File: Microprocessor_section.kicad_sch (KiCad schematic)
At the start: 13 parts, among them J15 Conn_01x06_Male, SW1 K2-1102SP-C4SC-04, U5 ESP32-WROOM-32D

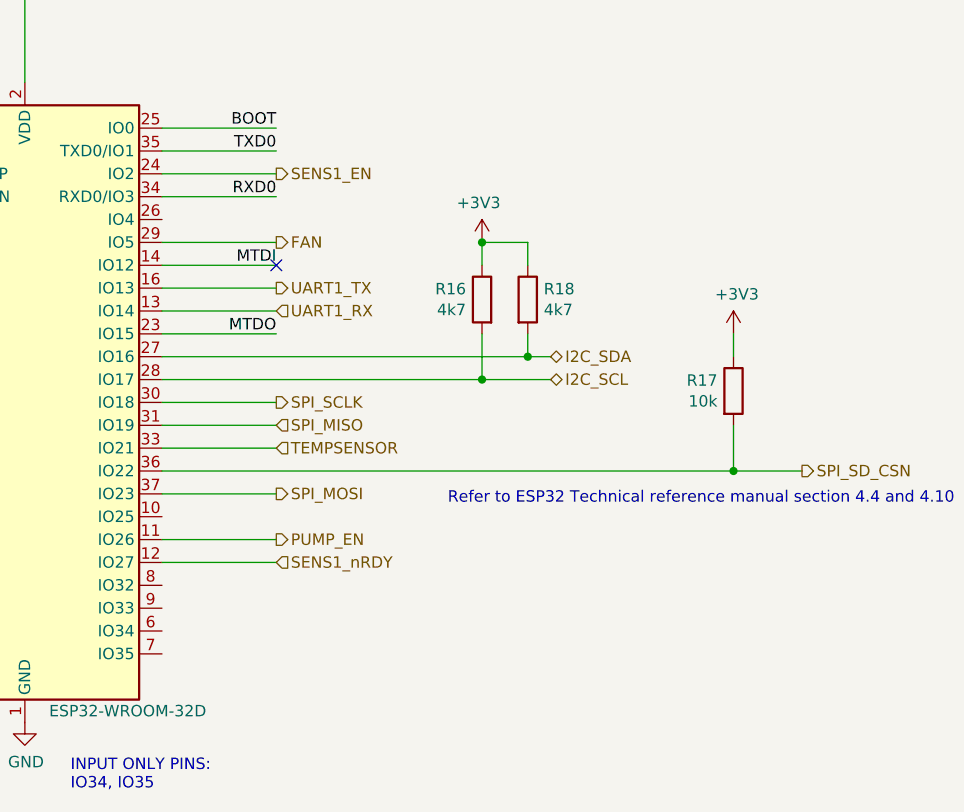
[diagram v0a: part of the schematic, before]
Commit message: Move to KiCad v6, redesign circuit for chamber
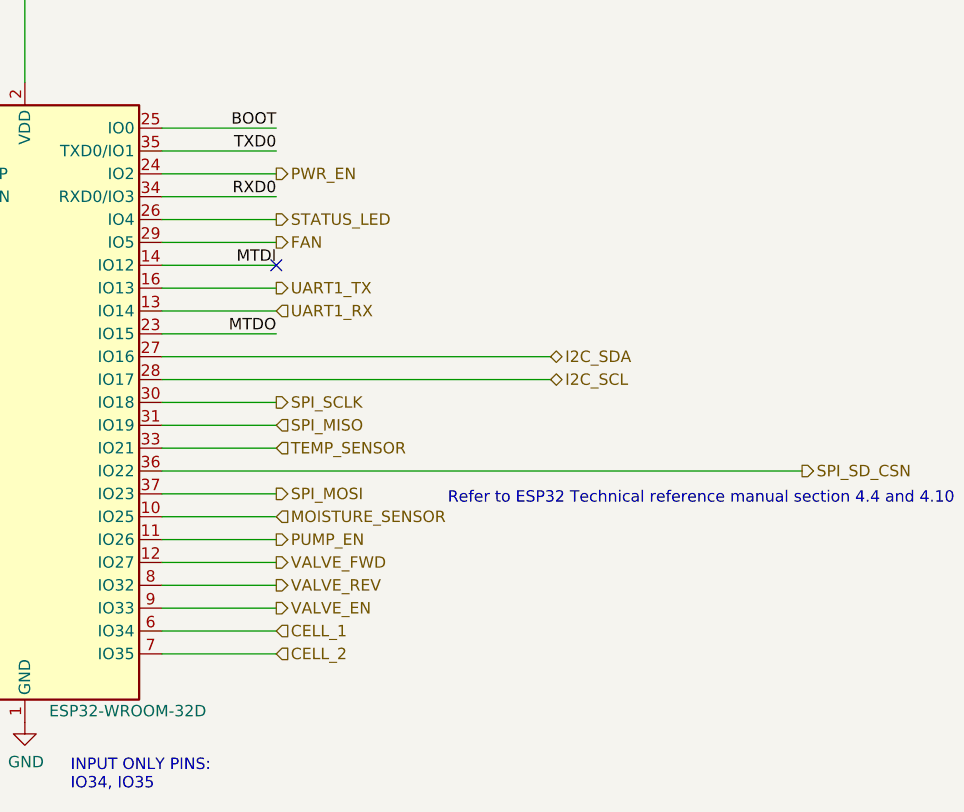
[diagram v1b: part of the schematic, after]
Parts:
- removed R16, R18: 4k7, Resistor_SMD:R_0603_1608Metric, symbol Device:R
- removed R17: 10k, Resistor_SMD:R_0603_1608Metric, symbol Device:R
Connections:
- net MOISTURE_SENSOR: now reaches U5.10 (IO25)
- net STATUS_LED: now reaches U5.26 (IO4)
- net CELL_1: now reaches U5.6 (IO34)
- net CELL_2: now reaches U5.7 (IO35)
- net VALVE_REV: now reaches U5.8 (IO32)
- net VALVE_EN: now reaches U5.9 (IO33)
- net SENS1_EN renamed PWR_EN
- net SENS1_nRDY renamed VALVE_FWD
- net TEMPSENSOR renamed TEMP_SENSOR

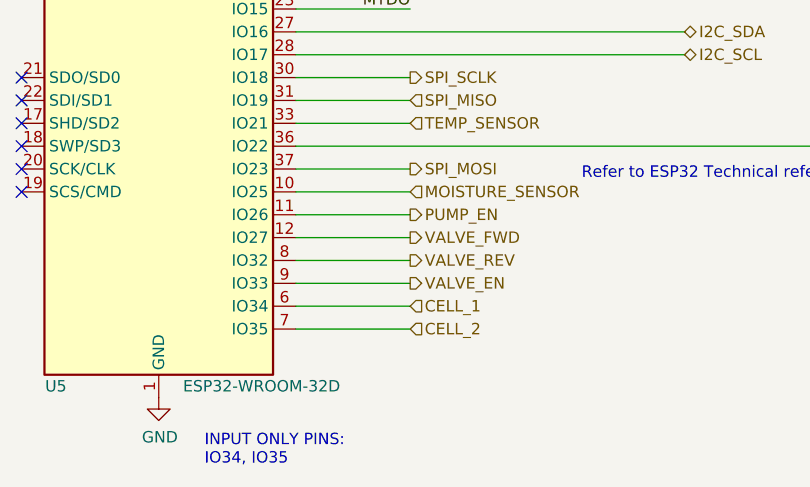
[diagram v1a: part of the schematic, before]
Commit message: Add test points, add JLC part numbers to JST XH connectors, clean up
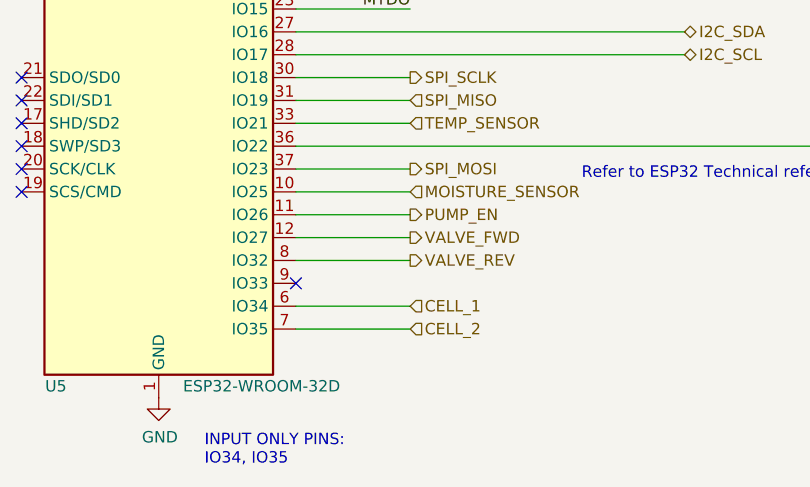
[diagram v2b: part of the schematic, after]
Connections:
- net VALVE_EN: no longer names the net of U5.9 (IO33)
- no-connect marks 9 -> 10
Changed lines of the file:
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@@
   (no_connect (at 149.86 78.74))
   (no_connect (at 149.86 104.14))
+  (no_connect (at 180.34 124.46))
   (wire (pts (xy 101.6 104.14) (xy 104.14 104.14))
     (stroke (width 0) (type default) (color 0 0 0 0))
@@
   )
   (wire (pts (xy 180.34 76.2) (xy 193.04 76.2))
-    (stroke (width 0) (type default) (color 0 0 0 0))
-  )
-  (wire (pts (xy 180.34 124.46) (xy 193.04 124.46))
     (stroke (width 0) (type default) (color 0 0 0 0))
   )
@@
     (effects (font (size 1.27 1.27)) (justify left))
   )
-  (hierarchical_label "VALVE_EN" (shape output) (at 193.04 124.46 0)
-    (effects (font (size 1.27 1.27)) (justify left))
-  )

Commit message: Finalize schematic
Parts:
- renumbered C19 to C7, C20 to C8, C21 to C9, J15 to J11, JP3 to JP1, JP4 to JP2, R14 to R12, R15 to R13, U5 to U2
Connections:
- net VALVE_2_FWD: now reaches U2.9 (IO33)
- net PUMP_EN renamed VALVE_2_REV
- net VALVE_FWD renamed VALVE_1_FWD
- net VALVE_REV renamed VALVE_1_REV
- no-connect marks 10 -> 9
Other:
- title: (none) -> CO2 Chamber - Microcontroller

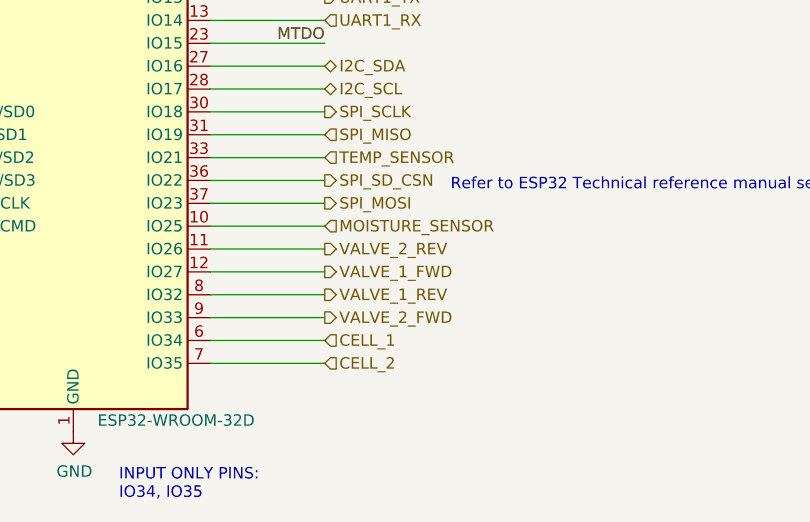
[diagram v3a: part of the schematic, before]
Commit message: Finish PCB layout
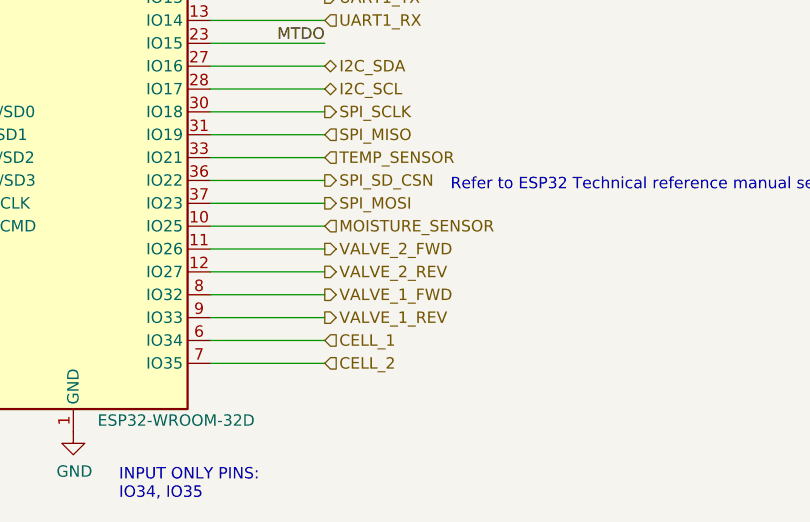
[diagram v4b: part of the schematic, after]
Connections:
- net VALVE_1_FWD: now also U2.8 (IO32); no longer U2.12 (IO27)
- net VALVE_1_REV: now also U2.9 (IO33); no longer U2.8 (IO32)
- net VALVE_2_FWD: now also U2.11 (IO26); no longer U2.9 (IO33)
- net VALVE_2_REV: now also U2.12 (IO27); no longer U2.11 (IO26)

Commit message: Checkpoint
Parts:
- removed J11: Conn_01x06_Male, Connector_PinHeader_2.54mm:PinHeader_1x06_P2.54mm_Vertical, symbol Connector:Conn_01x06_Male
- added J?: USB_B, co2_sensor_node:USB_MicroQTJ, symbol Connector:USB_B
- added JP?: USB_PWR_JP, Connector_PinHeader_2.54mm:PinHeader_1x02_P2.54mm_Vertical, symbol Connector:Conn_01x02_Male
- added Q? (x2): SS8050, Package_TO_SOT_SMD:SOT-23, symbol Device:Q_NPN_BCE
- added R? (x2): 12k, Resistor_SMD:R_0603_1608Metric, symbol Device:R
- added U?: CH340C, Package_SO:SOIC-16_3.9x9.9mm_P1.27mm, symbol Interface_USB:CH340C
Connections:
- net +3V3: now also U?.16 (VCC), U?.4 (V3)
- net BOOT: now also Q?.2 (C)
- net EN: now also Q?.2 (C)
- net GND: now also J?.4 (GND), U?.1 (GND)
- net RXD0: now also U?.2 (TXD)
- net TXD0: now also U?.3 (RXD)
- net CELL_1: no longer names the net of U2.6 (IO34)
- net CELL_2: no longer names the net of U2.7 (IO35)
- new net: J?.1 (VBUS), JP?.2 (Pin_2)
- new net: Q?.1 (B), R?.2 (x2)
- new net: Q?.3 (E), R?.1, U?.13 (~{DTR})
- new net: Q?.3 (E), R?.1, U?.14 (~{RTS})
- new net: J?.3 (D+), U?.5 (UD+)
- new net: J?.2 (D-), U?.6 (UD-)
- new net +BATT: JP?.1 (Pin_1)
- no-connect marks 9 -> 17
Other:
- note added: "Internal resistors"
- moved on the sheet: C7, C8, C9, JP1, JP2, R12, R13, SW1, U2

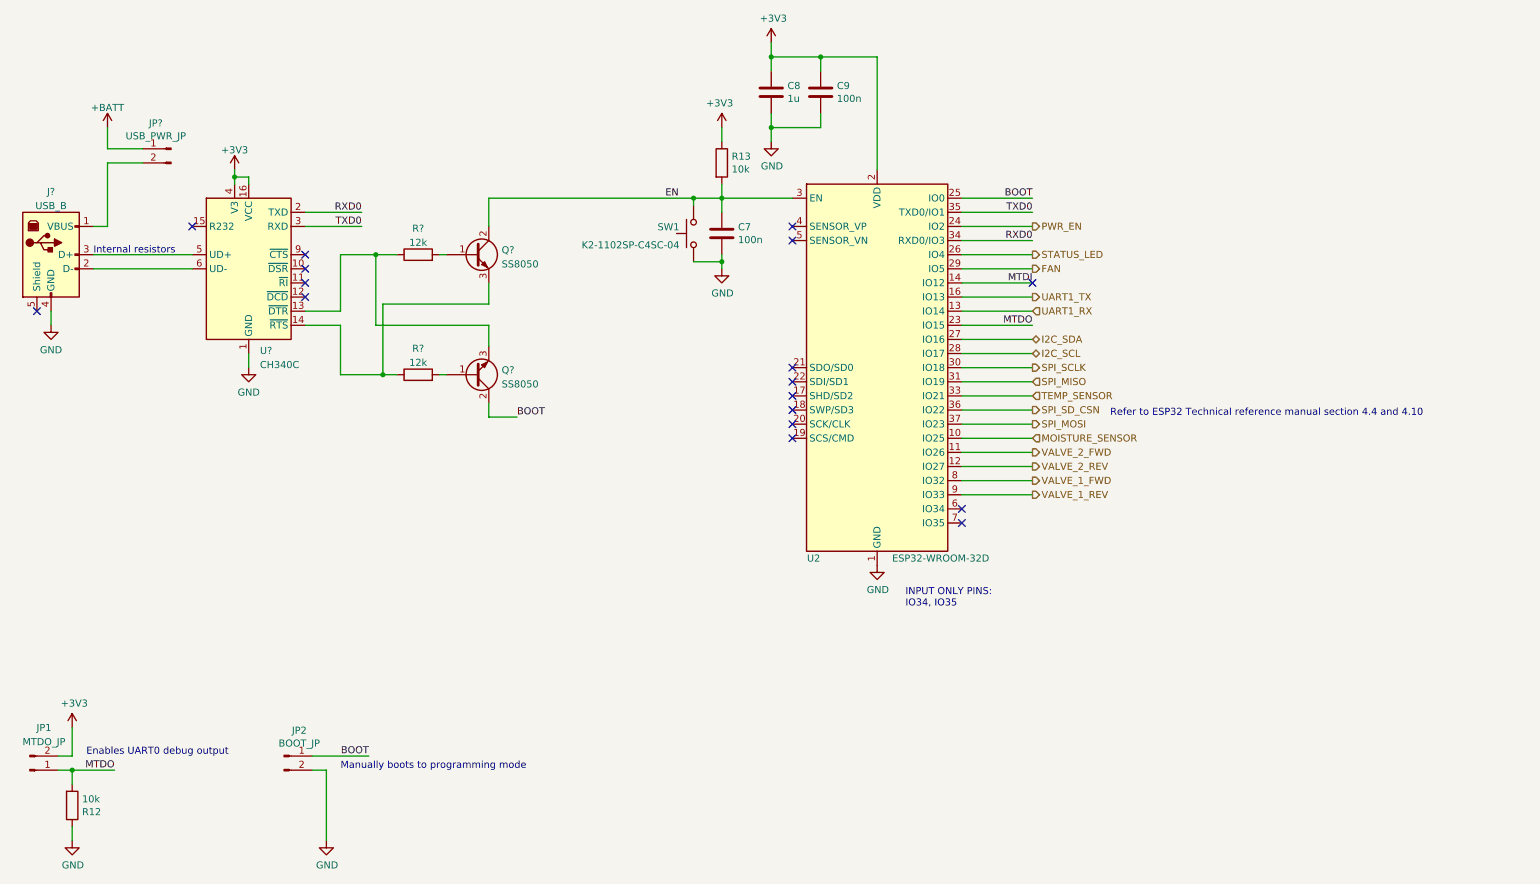
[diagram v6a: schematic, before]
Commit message: Finish rev. 2 schematic and begin PCB layout
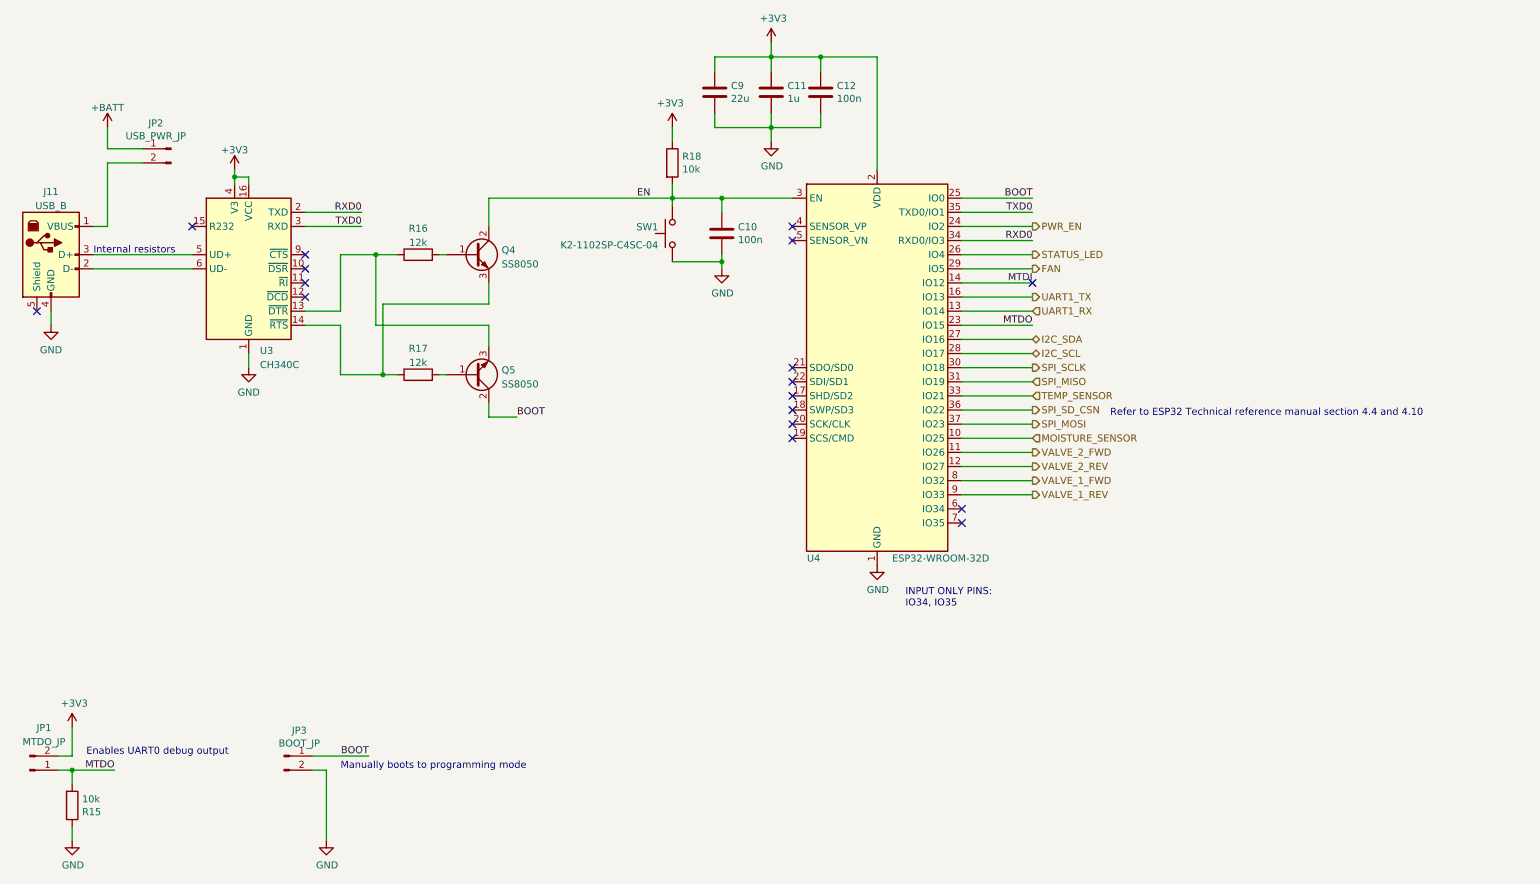
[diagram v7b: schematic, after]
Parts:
- added C9: 22u, Capacitor_SMD:C_0805_2012Metric, symbol Device:C
- gave numbers to parts that had none: 7
- renumbered C7 to C10, C8 to C11, C9 to C12, JP2 to JP3, R12 to R15, R13 to R18, U2 to U4
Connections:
- net +3V3: now also C9.1
- net GND: now also C9.2
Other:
- moved on the sheet: R18, SW1

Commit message: Add 5V boost converter and begin redesign of PCB
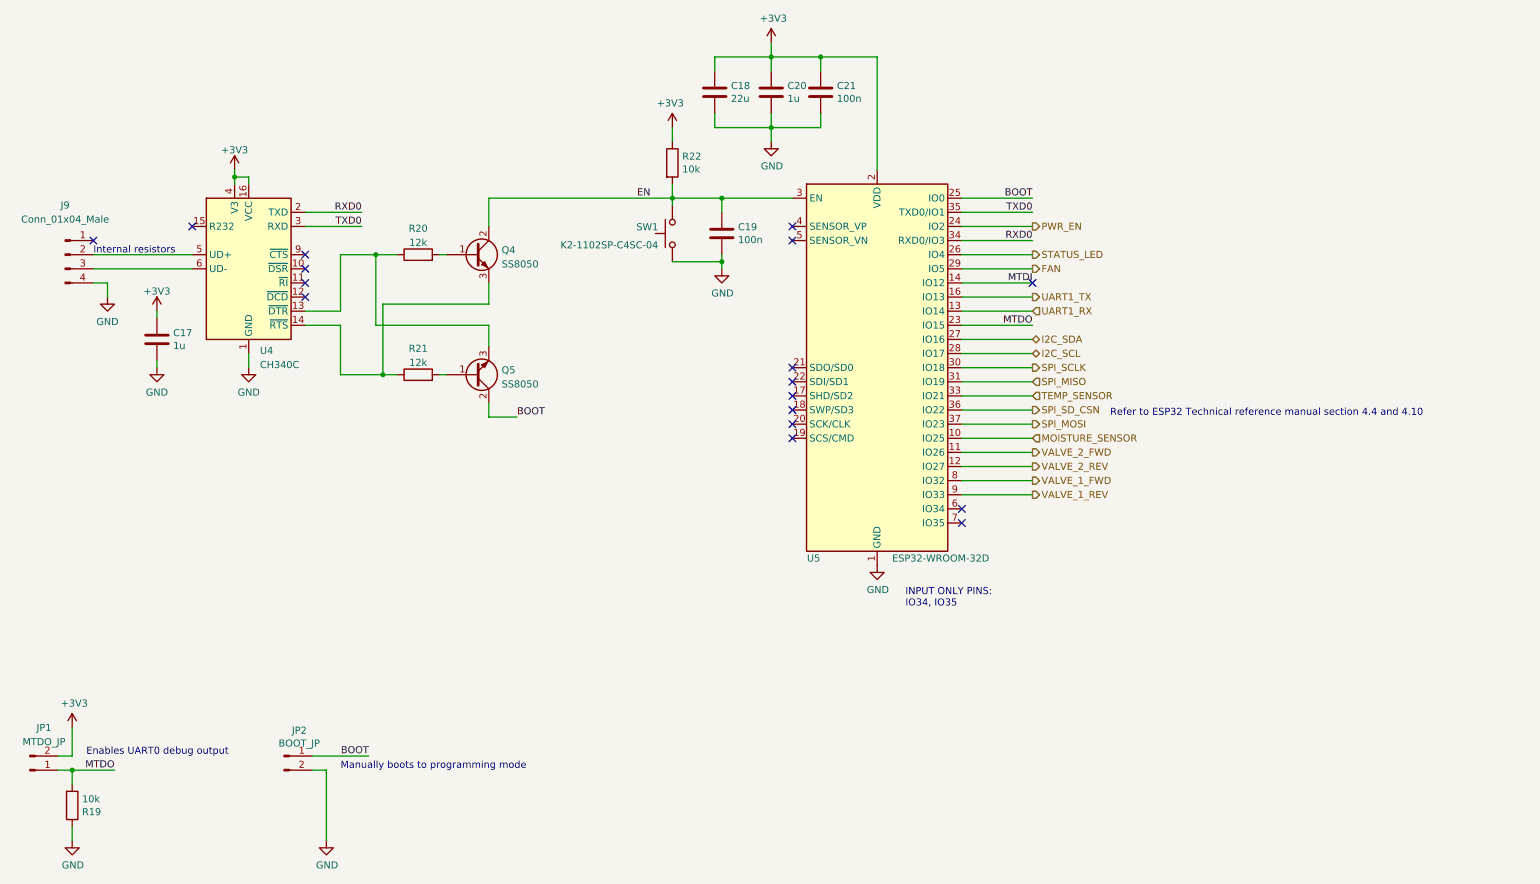
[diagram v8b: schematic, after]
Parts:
- removed J11: USB_B, co2_sensor_node:USB_MicroQTJ, symbol Connector:USB_B
- removed JP2: USB_PWR_JP, Connector_PinHeader_2.54mm:PinHeader_1x02_P2.54mm_Vertical, symbol Connector:Conn_01x02_Male
- added C17: 1u, Capacitor_SMD:C_0603_1608Metric, symbol Device:C
- added J9: Conn_01x04_Male, Connector_PinHeader_2.54mm:PinHeader_1x04_P2.54mm_Vertical, symbol Connector:Conn_01x04_Male
- renumbered C9 to C18, C10 to C19, C11 to C20, C12 to C21, JP3 to JP2, R15 to R19, R16 to R20, R17 to R21, R18 to R22, U3 to U4, U4 to U5
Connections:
- net +3V3: now also C17.1
- net GND: now also C17.2, J9.4 (Pin_4)
- net at U4.5 (UD+): now also J9.2 (Pin_2)
- net at U4.6 (UD-): now also J9.3 (Pin_3)
